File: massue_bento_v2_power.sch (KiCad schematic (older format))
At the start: 9 parts

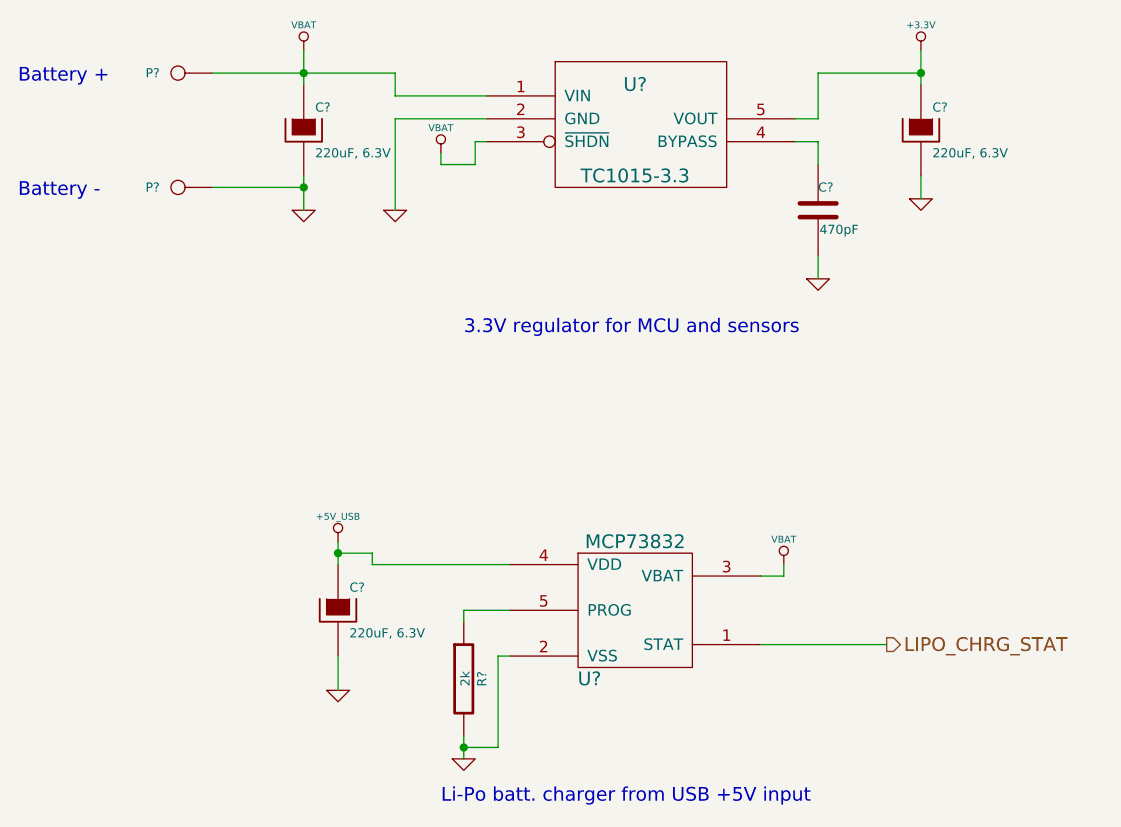
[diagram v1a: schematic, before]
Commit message: Fix: global annotation, fixed bugs to satisfy ERC
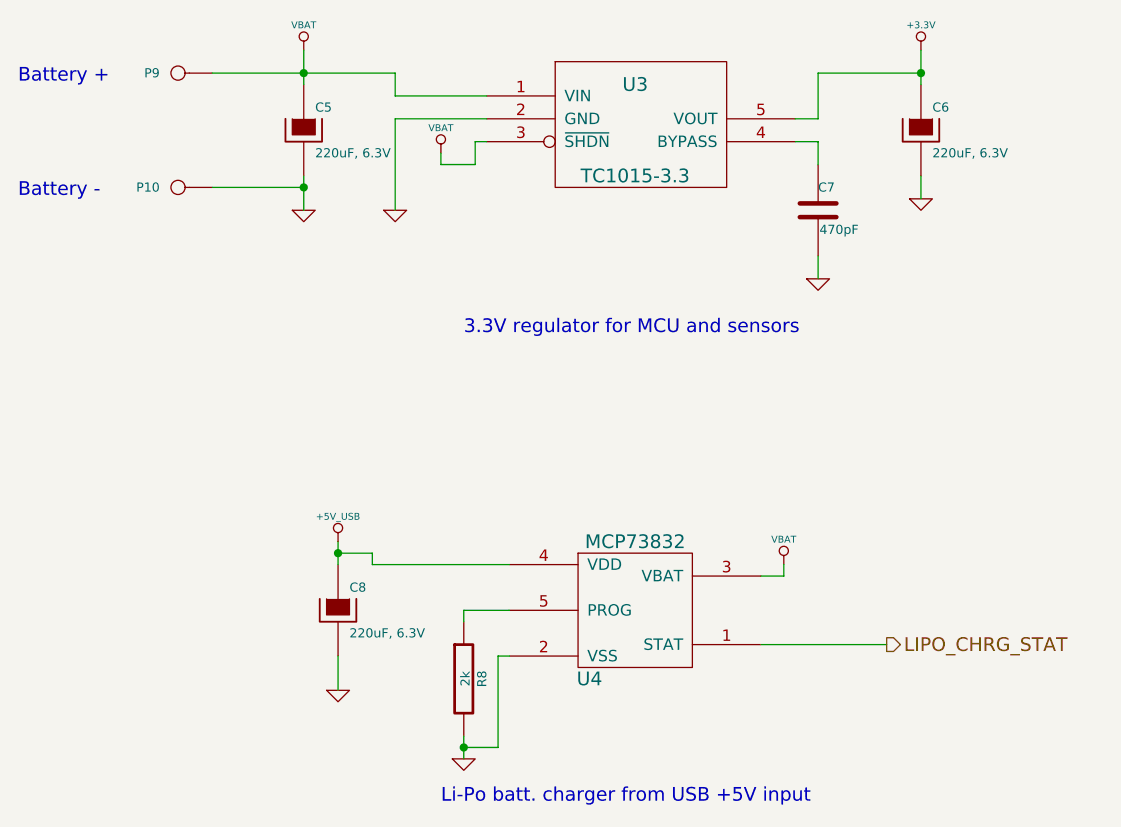
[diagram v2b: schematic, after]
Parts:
- gave numbers to parts that had none: 9
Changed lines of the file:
@@
 $EndDescr
 $Comp
-L CONN_1 P?
+L CONN_1 P9
 U 1 1 53A5845F
 P 2250 3000
-F 0 "P?" H 2330 3000 40  0000 L CNN
+F 0 "P9" H 2330 3000 40  0000 L CNN
 F 1 "CONN_1" H 2250 3055 30  0001 C CNN
 F 2 "" H 2250 3000 60  0000 C CNN
@@
 $EndComp
 $Comp
-L CONN_1 P?
+L CONN_1 P10
 U 1 1 53A58619
 P 2250 3500
-F 0 "P?" H 2330 3500 40  0000 L CNN
+F 0 "P10" H 2330 3500 40  0000 L CNN
 F 1 "CONN_1" H 2250 3555 30  0001 C CNN
 F 2 "" H 2250 3500 60  0000 C CNN
@@
 Battery -
 $Comp
-L CAPAPOL C?
+L CAPAPOL C5
 U 1 1 53A58774
 P 2800 3250
-F 0 "C?" H 2850 3350 40  0000 L CNN
+F 0 "C5" H 2850 3350 40  0000 L CNN
 F 1 "220uF, 6.3V" H 2850 3150 40  0000 L CNN
 F 2 "" H 2900 3100 30  0000 C CNN
@@
 	2800 3450 2800 3600
 $Comp
-L VBAT #PWR?
+L VBAT #PWR029
 U 1 1 53A58816
 P 2800 2900
-F 0 "#PWR?" H 2800 2960 30  0001 C CNN
+F 0 "#PWR029" H 2800 2960 30  0001 C CNN
 F 1 "VBAT" H 2800 3010 30  0000 C CNN
 F 2 "" H 2800 2900 60  0000 C CNN
@@
 Connection ~ 2800 3000
 $Comp
-L TC1015 U?
+L TC1015 U3
 U 1 1 53A588B2
 P 4250 3350
-F 0 "U?" H 4250 3650 60  0000 C CNN
+F 0 "U3" H 4250 3650 60  0000 C CNN
 F 1 "TC1015-3.3" H 4250 3250 60  0000 C CNN
 F 2 "" H 4250 3350 60  0000 C CNN
@@
 	3200 3100 3600 3100
 $Comp
-L GND #PWR?
+L GND #PWR030
 U 1 1 53A58A30
 P 2800 3600
-F 0 "#PWR?" H 2800 3600 30  0001 C CNN
+F 0 "#PWR030" H 2800 3600 30  0001 C CNN
 F 1 "GND" H 2800 3530 30  0001 C CNN
 F 2 "" H 2800 3600 60  0000 C CNN
@@
 Connection ~ 2800 3500
 $Comp
-L GND #PWR?
+L GND #PWR031
 U 1 1 53A58B18
 P 3200 3600
-F 0 "#PWR?" H 3200 3600 30  0001 C CNN
+F 0 "#PWR031" H 3200 3600 30  0001 C CNN
 F 1 "GND" H 3200 3530 30  0001 C CNN
 F 2 "" H 3200 3600 60  0000 C CNN
@@
 	3200 3200 3600 3200
 $Comp
-L VBAT #PWR?
+L VBAT #PWR032
 U 1 1 53A58B35
 P 3400 3350
-F 0 "#PWR?" H 3400 3410 30  0001 C CNN
+F 0 "#PWR032" H 3400 3410 30  0001 C CNN
 F 1 "VBAT" H 3400 3460 30  0000 C CNN
 F 2 "" H 3400 3350 60  0000 C CNN
@@
 	3550 3300 3600 3300
 $Comp
-L C C?
+L C C7
 U 1 1 53A58B7F
 P 5050 3600
-F 0 "C?" H 5050 3700 40  0000 L CNN
+F 0 "C7" H 5050 3700 40  0000 L CNN
 F 1 "470pF" H 5056 3515 40  0000 L CNN
 F 2 "" H 5088 3450 30  0000 C CNN
@@
 $EndComp
 $Comp
-L GND #PWR?
+L GND #PWR033
 U 1 1 53A58BFD
 P 5050 3900
-F 0 "#PWR?" H 5050 3900 30  0001 C CNN
+F 0 "#PWR033" H 5050 3900 30  0001 C CNN
 F 1 "GND" H 5050 3830 30  0001 C CNN
 F 2 "" H 5050 3900 60  0000 C CNN
@@
 	5050 3300 5050 3400
 $Comp
-L CAPAPOL C?
+L CAPAPOL C6
 U 1 1 53A58C7C
 P 5500 3250
-F 0 "C?" H 5550 3350 40  0000 L CNN
+F 0 "C6" H 5550 3350 40  0000 L CNN
 F 1 "220uF, 6.3V" H 5550 3150 40  0000 L CNN
 F 2 "" H 5600 3100 30  0000 C CNN
@@
 $EndComp
 $Comp
-L GND #PWR?
+L GND #PWR034
 U 1 1 53A58CF8
 P 5500 3550
-F 0 "#PWR?" H 5500 3550 30  0001 C CNN
+F 0 "#PWR034" H 5500 3550 30  0001 C CNN
 F 1 "GND" H 5500 3480 30  0001 C CNN
 F 2 "" H 5500 3550 60  0000 C CNN
@@
 	5500 2900 5500 3050
 $Comp
-L +3.3V #PWR?
+L +3.3V #PWR035
 U 1 1 53A58E01
 P 5500 2900
-F 0 "#PWR?" H 5500 2860 30  0001 C CNN
+F 0 "#PWR035" H 5500 2860 30  0001 C CNN
 F 1 "+3.3V" H 5500 3010 30  0000 C CNN
 F 2 "" H 5500 2900 60  0000 C CNN
@@
 3.3V regulator for MCU and sensors
 $Comp
-L MCP73832 U?
+L MCP73832 U4
 U 1 1 53A594EF
 P 4250 5350
-F 0 "U?" H 4050 5050 60  0000 C CNN
+F 0 "U4" H 4050 5050 60  0000 C CNN
 F 1 "MCP73832" H 4250 5650 60  0000 C CNN
 F 2 "" H 4250 5350 60  0000 C CNN
@@
 Li-Po batt. charger from USB +5V input
 $Comp
-L +5V_USB #PWR?
+L +5V_USB #PWR036
 U 1 1 53A58D1A
 P 2950 5050
-F 0 "#PWR?" H 2950 5110 40  0001 C CNN
+F 0 "#PWR036" H 2950 5110 40  0001 C CNN
 F 1 "+5V_USB" H 2950 5160 30  0000 C CNN
 F 2 "" H 2950 5050 60  0000 C CNN
@@
 $EndComp
 $Comp
-L CAPAPOL C?
+L CAPAPOL C8
 U 1 1 53A58E4B
 P 2950 5350
-F 0 "C?" H 3000 5450 40  0000 L CNN
+F 0 "C8" H 3000 5450 40  0000 L CNN
 F 1 "220uF, 6.3V" H 3000 5250 40  0000 L CNN
 F 2 "" H 3050 5200 30  0000 C CNN
@@
 	2950 5550 2950 5700
 $Comp
-L GND #PWR?
+L GND #PWR037
 U 1 1 53A5916F
 P 2950 5700
-F 0 "#PWR?" H 2950 5700 30  0001 C CNN
+F 0 "#PWR037" H 2950 5700 30  0001 C CNN
 F 1 "GND" H 2950 5630 30  0001 C CNN
 F 2 "" H 2950 5700 60  0000 C CNN
@@
 $EndComp
 $Comp
-L R R?
+L R R8
 U 1 1 53A591B6
 P 3500 5650
-F 0 "R?" V 3580 5650 40  0000 C CNN
+F 0 "R8" V 3580 5650 40  0000 C CNN
 F 1 "2k" V 3507 5651 40  0000 C CNN
 F 2 "" V 3430 5650 30  0000 C CNN
@@
 $EndComp
 $Comp
-L GND #PWR?
+L GND #PWR038
 U 1 1 53A5925A
 P 3500 6000
-F 0 "#PWR?" H 3500 6000 30  0001 C CNN
+F 0 "#PWR038" H 3500 6000 30  0001 C CNN
 F 1 "GND" H 3500 5930 30  0001 C CNN
 F 2 "" H 3500 6000 60  0000 C CNN
@@
 	3500 5350 3700 5350
 $Comp
-L VBAT #PWR?
+L VBAT #PWR039
 U 1 1 53A593EE
 P 4900 5150
-F 0 "#PWR?" H 4900 5210 30  0001 C CNN
+F 0 "#PWR039" H 4900 5210 30  0001 C CNN
 F 1 "VBAT" H 4900 5260 30  0000 C CNN
 F 2 "" H 4900 5150 60  0000 C CNN

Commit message: New : AT42 sensor
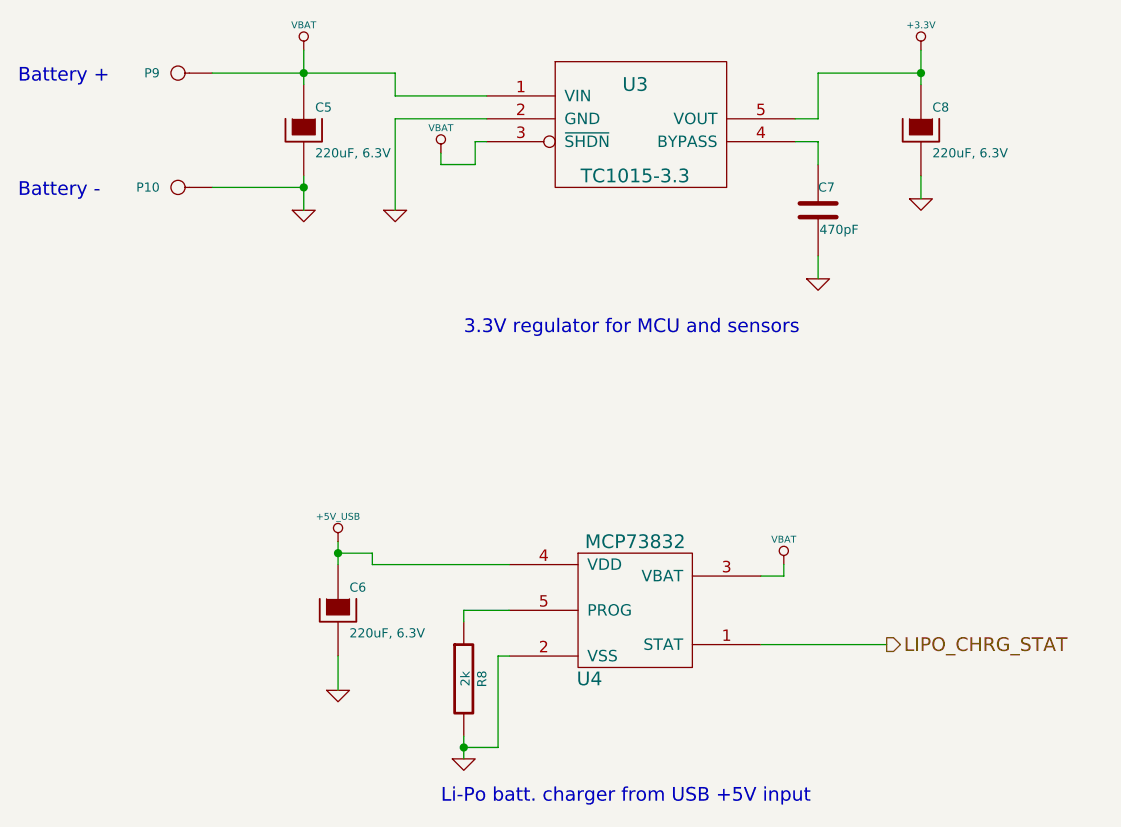
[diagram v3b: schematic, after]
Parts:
- renumbered C8 to C6, C6 to C8
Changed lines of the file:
@@
 EESchema Schematic File Version 2
 LIBS:power
+LIBS:tom_kicad
 LIBS:device
-LIBS:transistors
 LIBS:conn
-LIBS:linear
-LIBS:regul
-LIBS:74xx
-LIBS:cmos4000
-LIBS:adc-dac
-LIBS:memory
-LIBS:xilinx
-LIBS:special
-LIBS:microcontrollers
-LIBS:dsp
-LIBS:microchip
-LIBS:analog_switches
-LIBS:motorola
-LIBS:texas
-LIBS:intel
-LIBS:audio
-LIBS:interface
-LIBS:digital-audio
-LIBS:philips
-LIBS:display
-LIBS:cypress
-LIBS:siliconi
-LIBS:opto
-LIBS:atmel
-LIBS:contrib
-LIBS:valves
-LIBS:tom_kicad
 LIBS:massue_bento_v2-cache
 EELAYER 24 0
@@
 	2800 3450 2800 3600
 $Comp
-L VBAT #PWR029
+L VBAT #PWR030
 U 1 1 53A58816
 P 2800 2900
-F 0 "#PWR029" H 2800 2960 30  0001 C CNN
+F 0 "#PWR030" H 2800 2960 30  0001 C CNN
 F 1 "VBAT" H 2800 3010 30  0000 C CNN
 F 2 "" H 2800 2900 60  0000 C CNN
@@
 	3200 3100 3600 3100
 $Comp
-L GND #PWR030
+L GND #PWR031
 U 1 1 53A58A30
 P 2800 3600
-F 0 "#PWR030" H 2800 3600 30  0001 C CNN
+F 0 "#PWR031" H 2800 3600 30  0001 C CNN
 F 1 "GND" H 2800 3530 30  0001 C CNN
 F 2 "" H 2800 3600 60  0000 C CNN
@@
 Connection ~ 2800 3500
 $Comp
-L GND #PWR031
+L GND #PWR032
 U 1 1 53A58B18
 P 3200 3600
-F 0 "#PWR031" H 3200 3600 30  0001 C CNN
+F 0 "#PWR032" H 3200 3600 30  0001 C CNN
 F 1 "GND" H 3200 3530 30  0001 C CNN
 F 2 "" H 3200 3600 60  0000 C CNN
@@
 	3200 3200 3600 3200
 $Comp
-L VBAT #PWR032
+L VBAT #PWR033
 U 1 1 53A58B35
 P 3400 3350
-F 0 "#PWR032" H 3400 3410 30  0001 C CNN
+F 0 "#PWR033" H 3400 3410 30  0001 C CNN
 F 1 "VBAT" H 3400 3460 30  0000 C CNN
 F 2 "" H 3400 3350 60  0000 C CNN
@@
 $EndComp
 $Comp
-L GND #PWR033
+L GND #PWR034
 U 1 1 53A58BFD
 P 5050 3900
-F 0 "#PWR033" H 5050 3900 30  0001 C CNN
+F 0 "#PWR034" H 5050 3900 30  0001 C CNN
 F 1 "GND" H 5050 3830 30  0001 C CNN
 F 2 "" H 5050 3900 60  0000 C CNN
@@
 	5050 3300 5050 3400
 $Comp
-L CAPAPOL C6
+L CAPAPOL C8
 U 1 1 53A58C7C
 P 5500 3250
-F 0 "C6" H 5550 3350 40  0000 L CNN
+F 0 "C8" H 5550 3350 40  0000 L CNN
 F 1 "220uF, 6.3V" H 5550 3150 40  0000 L CNN
 F 2 "" H 5600 3100 30  0000 C CNN
@@
 $EndComp
 $Comp
-L GND #PWR034
+L GND #PWR035
 U 1 1 53A58CF8
 P 5500 3550
-F 0 "#PWR034" H 5500 3550 30  0001 C CNN
+F 0 "#PWR035" H 5500 3550 30  0001 C CNN
 F 1 "GND" H 5500 3480 30  0001 C CNN
 F 2 "" H 5500 3550 60  0000 C CNN
@@
 	5500 2900 5500 3050
 $Comp
-L +3.3V #PWR035
+L +3.3V #PWR036
 U 1 1 53A58E01
 P 5500 2900
-F 0 "#PWR035" H 5500 2860 30  0001 C CNN
+F 0 "#PWR036" H 5500 2860 30  0001 C CNN
 F 1 "+3.3V" H 5500 3010 30  0000 C CNN
 F 2 "" H 5500 2900 60  0000 C CNN
@@
 Li-Po batt. charger from USB +5V input
 $Comp
-L +5V_USB #PWR036
+L +5V_USB #PWR037
 U 1 1 53A58D1A
 P 2950 5050
-F 0 "#PWR036" H 2950 5110 40  0001 C CNN
+F 0 "#PWR037" H 2950 5110 40  0001 C CNN
 F 1 "+5V_USB" H 2950 5160 30  0000 C CNN
 F 2 "" H 2950 5050 60  0000 C CNN
@@
 $EndComp
 $Comp
-L CAPAPOL C8
+L CAPAPOL C6
 U 1 1 53A58E4B
 P 2950 5350
-F 0 "C8" H 3000 5450 40  0000 L CNN
+F 0 "C6" H 3000 5450 40  0000 L CNN
 F 1 "220uF, 6.3V" H 3000 5250 40  0000 L CNN
 F 2 "" H 3050 5200 30  0000 C CNN
@@
 	2950 5550 2950 5700
 $Comp
-L GND #PWR037
+L GND #PWR038
 U 1 1 53A5916F
 P 2950 5700
-F 0 "#PWR037" H 2950 5700 30  0001 C CNN
+F 0 "#PWR038" H 2950 5700 30  0001 C CNN
 F 1 "GND" H 2950 5630 30  0001 C CNN
 F 2 "" H 2950 5700 60  0000 C CNN
@@
 $EndComp
 $Comp
-L GND #PWR038
+L GND #PWR039
 U 1 1 53A5925A
 P 3500 6000
-F 0 "#PWR038" H 3500 6000 30  0001 C CNN
+F 0 "#PWR039" H 3500 6000 30  0001 C CNN
 F 1 "GND" H 3500 5930 30  0001 C CNN
 F 2 "" H 3500 6000 60  0000 C CNN
@@
 	3500 5350 3700 5350
 $Comp
-L VBAT #PWR039
+L VBAT #PWR040
 U 1 1 53A593EE
 P 4900 5150
-F 0 "#PWR039" H 4900 5210 30  0001 C CNN
+F 0 "#PWR040" H 4900 5210 30  0001 C CNN
 F 1 "VBAT" H 4900 5260 30  0000 C CNN
 F 2 "" H 4900 5150 60  0000 C CNN

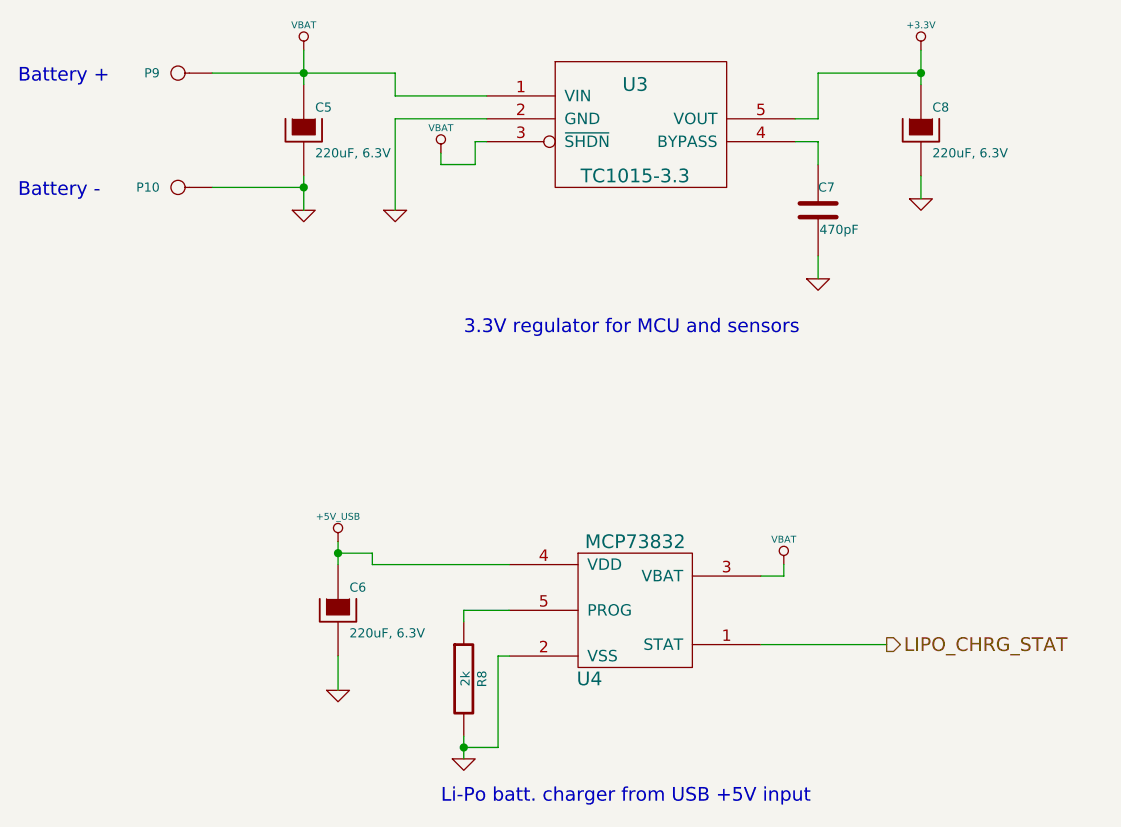
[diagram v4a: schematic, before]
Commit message: New: first routing for almost all signals
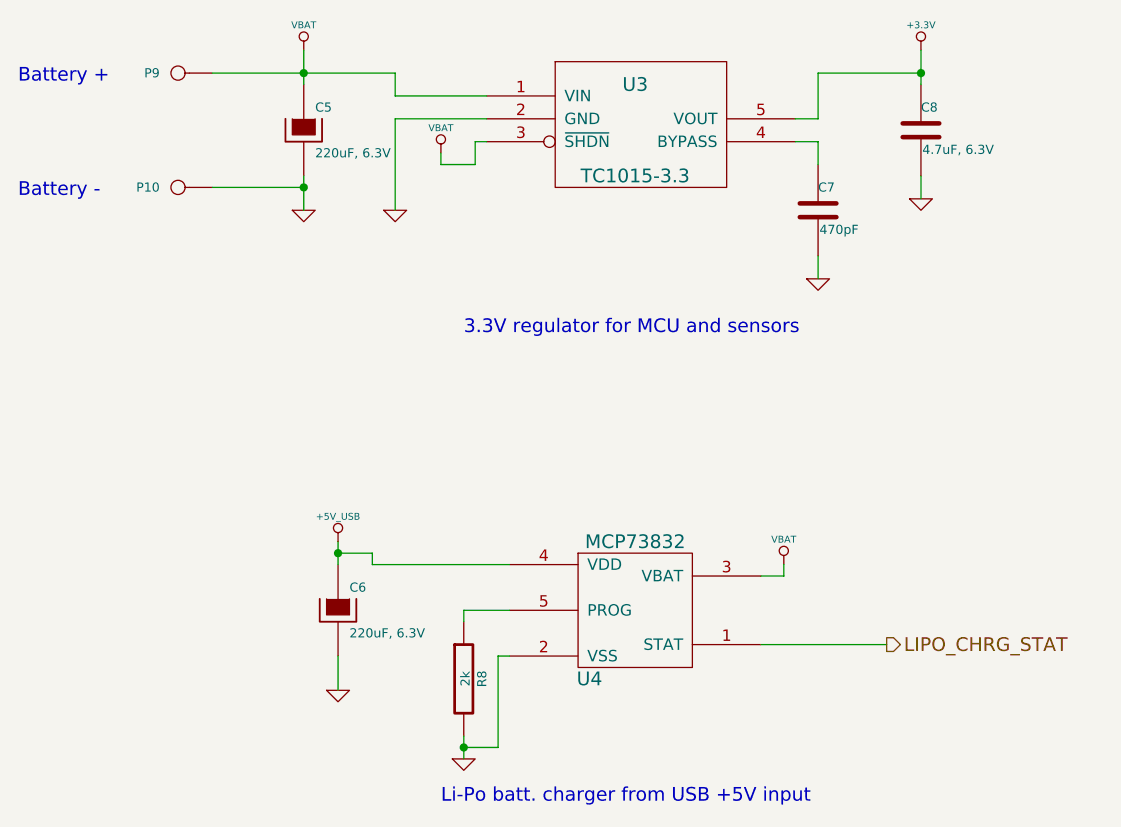
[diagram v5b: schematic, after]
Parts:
- removed C8: 220uF, 6.3V, symbol CAPAPOL
- added C8: 4.7uF, 6.3V, symbol C
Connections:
- net +3.3V: now also C8.1
- net GND: now also C8.2
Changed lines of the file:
@@
 	5050 3300 5050 3400
-$Comp
-L CAPAPOL C8
-U 1 1 53A58C7C
-P 5500 3250
-F 0 "C8" H 5550 3350 40  0000 L CNN
-F 1 "220uF, 6.3V" H 5550 3150 40  0000 L CNN
-F 2 "" H 5600 3100 30  0000 C CNN
-F 3 "" H 5500 3250 300 0000 C CNN
-	1    5500 3250
-	1    0    0    -1
-$EndComp
 $Comp
 L GND #PWR034
@@
 $EndComp
 Wire Wire Line
-	3500 6000 3500 5900
+	3500 5900 3500 6000
 Wire Wire Line
 	3500 5950 3650 5950
@@
 Text HLabel 5350 5500 2    60   Output ~ 0
 LIPO_CHRG_STAT
+$Comp
+L C C8
+U 1 1 53AFED1B
+P 5500 3250
+F 0 "C8" H 5500 3350 40  0000 L CNN
+F 1 "4.7uF, 6.3V" H 5506 3165 40  0000 L CNN
+F 2 "" H 5538 3100 30  0000 C CNN
+F 3 "" H 5500 3250 60  0000 C CNN
+	1    5500 3250
+	1    0    0    -1
+$EndComp
 $EndSCHEMATC
